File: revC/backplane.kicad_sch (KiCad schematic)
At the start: 40 parts, among them J101 BURN WIRES, J103 SEP1 & SEP2, J104 SEP3 & SEP4, J105 +X SOLAR PANEL, J106 -X SOLAR PANEL, J107 +Y SOLAR PANEL, J108 -Z SOLAR PANEL, J200_1 HSEC8-160-01-S-DV-A-K-TR, J200_2 HSEC8-160-01-S-DV-A-K-TR, J200_3 HSEC8-160-01-S-DV-A-K-TR, J200_4 HSEC8-160-01-S-DV-A-K-TR, J200_5 HSEC8-160-01-S-DV-A-K-TR, J200_6 HSEC8-160-01-S-DV-A-K-TR, J200_7 HSEC8-160-01-S-DV-A-K-TR, J200_8 HSEC8-160-01-S-DV-A-K-TR, J300 Breakout Connector, J301 Breakout Connector, SW100 RESET, SW101 RESET

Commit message: updated layout for fm.
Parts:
- removed J101: BURN WIRES, CubeSat_Backplane:SAMTEC_T1M-04-F-SV-L, symbol Connector_Generic:Conn_01x04
- added R604: 0R, Resistor_SMD:R_0402_1005Metric, symbol backplane-rescue:R_US-Device
- C100, C101, C102, C103, C104, C105: value 0.1uF -> 10nF; Manufacturer Part Number 1 GRM155R71C104KA88D -> CGA2B3X7S2A103K050BB
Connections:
- net H1-1 is gone; now on net SEP1_RET: J200_1.9 (Pin_9), J200_2.9 (Pin_9), J200_3.9 (Pin_9), J200_4.9 (Pin_9), J200_5.9 (Pin_9), J200_6.9 (Pin_9), J200_7.9 (Pin_9), J200_8.9 (Pin_9), J300.5 (Pin_5)
- net H1-16 is gone; now on net RBF_RET: J200_1.38 (Pin_38), J200_2.38 (Pin_38), J200_3.38 (Pin_38), J200_4.38 (Pin_38), J200_5.38 (Pin_38), J200_6.38 (Pin_38), J200_7.38 (Pin_38), J200_8.38 (Pin_38), J300.20 (Pin_20)
- net H1-2 is gone; now on net SEP2_RET: J200_1.10 (Pin_10), J200_2.10 (Pin_10), J200_3.10 (Pin_10), J200_4.10 (Pin_10), J200_5.10 (Pin_10), J200_6.10 (Pin_10), J200_7.10 (Pin_10), J200_8.10 (Pin_10), J300.6 (Pin_6)
- net H2-5 is gone; now on net GND: J200_1.19 (Pin_19), J200_2.19 (Pin_19), J200_3.19 (Pin_19), J200_4.19 (Pin_19), J200_5.19 (Pin_19), J200_6.19 (Pin_19), J200_7.19 (Pin_19), J200_8.19 (Pin_19), J301.9 (Pin_9)
- net H2-6 is gone; now on net GND: J200_1.20 (Pin_20), J200_2.20 (Pin_20), J200_3.20 (Pin_20), J200_4.20 (Pin_20), J200_5.20 (Pin_20), J200_6.20 (Pin_20), J200_7.20 (Pin_20), J200_8.20 (Pin_20), J301.10 (Pin_10)
- net DIN_LED_1: now also J200_1.14 (Pin_14), J301.8 (Pin_8); no longer J200_1.100 (Pin_100), J300.52 (Pin_52)
- net DIN_LED_2: now also J200_1.16 (Pin_16), J200_2.14 (Pin_14); no longer J200_1.102 (Pin_102), J200_2.100 (Pin_100)
- net DIN_LED_3: now also J200_2.16 (Pin_16), J200_3.14 (Pin_14); no longer J200_2.102 (Pin_102), J200_3.100 (Pin_100)
- net DIN_LED_4: now also J200_3.16 (Pin_16), J200_4.14 (Pin_14); no longer J200_3.102 (Pin_102), J200_4.100 (Pin_100)
- net DIN_LED_5: now also J200_4.16 (Pin_16), J200_5.14 (Pin_14); no longer J200_4.102 (Pin_102), J200_5.100 (Pin_100)
- net DIN_LED_6: now also J200_5.16 (Pin_16), J200_6.14 (Pin_14); no longer J200_5.102 (Pin_102), J200_6.100 (Pin_100)
- net DIN_LED_7: now also J200_6.16 (Pin_16), J200_7.14 (Pin_14); no longer J200_6.102 (Pin_102), J200_7.100 (Pin_100)
- net DIN_LED_8: now also J200_7.16 (Pin_16), J200_8.14 (Pin_14), R604.2; no longer J200_7.102 (Pin_102), J200_8.100 (Pin_100)
- net RBF_RET: no longer J200_1.107 (Pin_107), J200_2.107 (Pin_107), J200_3.107 (Pin_107), J200_4.107 (Pin_107), J200_5.107 (Pin_107), J200_6.107 (Pin_107), J200_7.107 (Pin_107), J200_8.107 (Pin_107), J301.53 (Pin_53)
- net SEP1_RET: no longer J200_1.109 (Pin_109), J200_2.109 (Pin_109), J200_3.109 (Pin_109), J200_4.109 (Pin_109), J200_5.109 (Pin_109), J200_6.109 (Pin_109), J200_7.109 (Pin_109), J200_8.109 (Pin_109), J300.55 (Pin_55)
- net SEP2_RET: no longer J200_1.110 (Pin_110), J200_2.110 (Pin_110), J200_3.110 (Pin_110), J200_4.110 (Pin_110), J200_5.110 (Pin_110), J200_6.110 (Pin_110), J200_7.110 (Pin_110), J200_8.110 (Pin_110), J300.56 (Pin_56)
- net BP_LED_PWR renamed H1-49
- net DIN_BO_LED renamed DIN_LED_BO
- net DIN_LED_BO: now also J300.8 (Pin_8); no longer J301.50 (Pin_50)
- net DIN_BP_LED renamed H1-48
- net H1-48: now also J200_1.102 (Pin_102), J200_2.102 (Pin_102), J200_3.102 (Pin_102), J200_4.102 (Pin_102), J200_5.102 (Pin_102), J200_6.102 (Pin_102), J200_7.102 (Pin_102), J300.52 (Pin_52)
- net H1-3 renamed ~{LED_EN}
- removed net H1-4: J200_1.14 (Pin_14), J200_2.14 (Pin_14), J200_3.14 (Pin_14), J200_4.14 (Pin_14), J200_5.14 (Pin_14), J200_6.14 (Pin_14), J200_7.14 (Pin_14), J200_8.14 (Pin_14), J300.8 (Pin_8)
- net H2-3 renamed LED_PWR
- removed net H2-4: J200_1.16 (Pin_16), J200_2.16 (Pin_16), J200_3.16 (Pin_16), J200_4.16 (Pin_16), J200_5.16 (Pin_16), J200_6.16 (Pin_16), J200_7.16 (Pin_16), J200_8.16 (Pin_16), J301.8 (Pin_8)
- net ~{BP_LED_EN} renamed H1-50
- new net DIN_LED_BP: J200_8.16 (Pin_16), R604.1
- new net H1-51: J200_1.109 (Pin_109), J200_2.109 (Pin_109), J200_3.109 (Pin_109), J200_4.109 (Pin_109), J200_5.109 (Pin_109), J200_6.109 (Pin_109), J200_7.109 (Pin_109), J200_8.109 (Pin_109), J300.55 (Pin_55)
- new net H1-52: J200_1.110 (Pin_110), J200_2.110 (Pin_110), J200_3.110 (Pin_110), J200_4.110 (Pin_110), J200_5.110 (Pin_110), J200_6.110 (Pin_110), J200_7.110 (Pin_110), J200_8.110 (Pin_110), J300.56 (Pin_56)
- new net H2-46: J200_1.100 (Pin_100), J200_2.100 (Pin_100), J200_3.100 (Pin_100), J200_4.100 (Pin_100), J200_5.100 (Pin_100), J200_6.100 (Pin_100), J200_7.100 (Pin_100), J200_8.100 (Pin_100), J301.50 (Pin_50)
- new net H2-49: J200_1.107 (Pin_107), J200_2.107 (Pin_107), J200_3.107 (Pin_107), J200_4.107 (Pin_107), J200_5.107 (Pin_107), J200_6.107 (Pin_107), J200_7.107 (Pin_107), J200_8.107 (Pin_107), J301.53 (Pin_53)
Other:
- note added: "Breakout Connectors"
- note added: "Breakout connectors are only used for ground testing. 2.1A per pin. trace width: 0.25mm Via: 0.2mm drill, 0.5mm dia."
- note added: "Bus Connectors"
- note added: "Configure pin on controller to have an internal pull up SELF_TEST input."
- note added: "DIN_LED-DOUT_LED jumpers install to bypass or stop data signal."
- note added: "LEDs"
- note added: "SK6812-EC3210 (NeoPixel) LEDs. Pull enable high at controller. LEDs are configured in a ring, with jumpers to bypass or terminate the data signal."
- note added: "Seperation Switch Connectors"
- note added: "Six #4 Mounting Holes for Sierra Lobo 1.5U cubesat structure."
- note added: "To connect breakout, connect male headers on rear of backplane then connect breakout harness (Samtec SFSD-30-28-G-15.74-D-NUS) Ensure harness is of "NUS" option for connecting to breakout."
- note removed: "BACKPLANE BREAKOUT CONNECTOR IS ONLY USED FOR GROUND TESTING CONTACT RATING 2.1A PER PIN TRACE WIDTH: 0.25mm VIA SIZE: 0.2mm DRILL, 0.5mm PAD"
- note removed: "Burn Wire Connector"
- note removed: "Configure pin on PPM/Motherboard/mainboard to have an internal pull up for H1-47 (USER0) for SELF_TEST input."
- note removed: "DIN_LED-DOUT_LED jumpers install when not used per backplane connector."
- note removed: "Default Bus Connectors"
- note removed: "End of CSK Bus"
- note removed: "First 104 pins follow pumpkin CSK bus (Rev E) pins Some user and IO pins have been assigned by SLI ( that are not used by any other peripherials )"
- note removed: "PCB BOTTOM"
- note removed: "PCB TOP"
- note removed: "Seperation Switch Connector"
- note removed: "breakout connectors are spaced such that the breakout BOARD thickness is 3.2mm!!"
- moved on the sheet: C100, C101, C102, C103, C104, C105, J103, J104, J105, J106, J107, J108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

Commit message: working post-review changes
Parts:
- added J1: SSM-102-L-SV-BE-TR, symbol Connector_Generic:Conn_01x02
- added J109: NTC1, SierraLobo:SAMTEC_T1M-02-F-SV-L-P, symbol Connector_Generic:Conn_01x02
- added J110: NTC2, SierraLobo:SAMTEC_T1M-02-F-SV-L-P, symbol Connector_Generic:Conn_01x02
- added J111: NTC3, SierraLobo:SAMTEC_T1M-02-F-SV-L-P, symbol Connector_Generic:Conn_01x02
- added J112: NTC4, SierraLobo:SAMTEC_T1M-02-F-SV-L-P, symbol Connector_Generic:Conn_01x02
- added J113: BURN1, SierraLobo:SAMTEC_T1M-04-F-SV-L, symbol Connector_Generic:Conn_01x04
- added J114: BURN2, SierraLobo:SAMTEC_T1M-04-F-SV-L, symbol Connector_Generic:Conn_01x04
- J103, J104: Manufacturer Part Number 1 (none) -> T1M-04-F-SV-L
- J105, J106, J107, J108: Manufacturer Part Number 1 (none) -> T1M-06-F-SV-L
- J200_1, J200_2, J200_3, J200_4, J200_5, J200_6, J200_7, J200_8: value HSEC8-160-01-S-DV-A-K-TR -> HTEC8-160-01-L-DV-A; Manufacturer Part Number 1 HSEC8-160-01-S-DV-A-K-TR -> HTEC8-160-01-L-DV-A
- MH100, MH101, MH102, MH103, MH104, MH105: Manufacturer Part Number 1 #4 Socket Head -> (none); now left out of the parts list
- R604: now not fitted
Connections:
- net H2-13 is gone; now on net GND: J200_1.35 (Pin_35), J200_2.35 (Pin_35), J200_3.35 (Pin_35), J200_4.35 (Pin_35), J200_5.35 (Pin_35), J200_6.35 (Pin_35), J200_7.35 (Pin_35), J200_8.35 (Pin_35), J301.17 (Pin_17)
- net H2-14 is gone; now on net GND: J200_1.36 (Pin_36), J200_2.36 (Pin_36), J200_3.36 (Pin_36), J200_4.36 (Pin_36), J200_5.36 (Pin_36), J200_6.36 (Pin_36), J200_7.36 (Pin_36), J200_8.36 (Pin_36), J301.18 (Pin_18)
- net H2-2 is gone; now on net SEP2_RET: J200_1.12 (Pin_12), J200_2.12 (Pin_12), J200_3.12 (Pin_12), J200_4.12 (Pin_12), J200_5.12 (Pin_12), J200_6.12 (Pin_12), J200_7.12 (Pin_12), J200_8.12 (Pin_12), J301.6 (Pin_6)
- net GND: now also J109.2 (Pin_2), J110.2 (Pin_2), J111.2 (Pin_2), J112.2 (Pin_2), J113.3 (Pin_3), J113.4 (Pin_4), J114.3 (Pin_3), J114.4 (Pin_4); no longer J200_1.19 (Pin_19), J200_1.20 (Pin_20), J200_2.19 (Pin_19), J200_2.20 (Pin_20), J200_3.19 (Pin_19), J200_3.20 (Pin_20), J200_4.19 (Pin_19), J200_4.20 (Pin_20), J200_5.19 (Pin_19), J200_5.20 (Pin_20), J200_6.19 (Pin_19), J200_6.20 (Pin_20), J200_7.19 (Pin_19), J200_7.20 (Pin_20), J200_8.19 (Pin_19), J200_8.20 (Pin_20), J301.10 (Pin_10), J301.9 (Pin_9)
- net RBF: now also J1.1 (Pin_1)
- net RBF_RET: now also J1.2 (Pin_2)
- net SEP1_RET: now also J200_1.13 (Pin_13), J200_2.13 (Pin_13), J200_3.13 (Pin_13), J200_4.13 (Pin_13), J200_5.13 (Pin_13), J200_6.13 (Pin_13), J200_7.13 (Pin_13), J200_8.13 (Pin_13), J300.7 (Pin_7); no longer J200_1.9 (Pin_9), J200_2.9 (Pin_9), J200_3.9 (Pin_9), J200_4.9 (Pin_9), J200_5.9 (Pin_9), J200_6.9 (Pin_9), J200_7.9 (Pin_9), J200_8.9 (Pin_9), J300.5 (Pin_5)
- net SEP2_RET: no longer J200_1.10 (Pin_10), J200_2.10 (Pin_10), J200_3.10 (Pin_10), J200_4.10 (Pin_10), J200_5.10 (Pin_10), J200_6.10 (Pin_10), J200_7.10 (Pin_10), J200_8.10 (Pin_10), J300.6 (Pin_6)
- net ~{LED_EN}: no longer J200_1.13 (Pin_13), J200_2.13 (Pin_13), J200_3.13 (Pin_13), J200_4.13 (Pin_13), J200_5.13 (Pin_13), J200_6.13 (Pin_13), J200_7.13 (Pin_13), J200_8.13 (Pin_13), J300.7 (Pin_7)
- net H2-7 renamed NTC3
- net NTC3: now also J111.1 (Pin_1)
- net H2-8 renamed NTC4
- net NTC4: now also J112.1 (Pin_1)
- new net NTC1: J109.1 (Pin_1), J200_1.19 (Pin_19), J200_2.19 (Pin_19), J200_3.19 (Pin_19), J200_4.19 (Pin_19), J200_5.19 (Pin_19), J200_6.19 (Pin_19), J200_7.19 (Pin_19), J200_8.19 (Pin_19), J301.9 (Pin_9)
- new net NTC2: J110.1 (Pin_1), J200_1.20 (Pin_20), J200_2.20 (Pin_20), J200_3.20 (Pin_20), J200_4.20 (Pin_20), J200_5.20 (Pin_20), J200_6.20 (Pin_20), J200_7.20 (Pin_20), J200_8.20 (Pin_20), J301.10 (Pin_10)
- new net VBURN1: J113.1 (Pin_1), J113.2 (Pin_2), J200_1.9 (Pin_9), J200_2.9 (Pin_9), J200_3.9 (Pin_9), J200_4.9 (Pin_9), J200_5.9 (Pin_9), J200_6.9 (Pin_9), J200_7.9 (Pin_9), J200_8.9 (Pin_9), J300.5 (Pin_5)
- new net VBURN2: J114.1 (Pin_1), J114.2 (Pin_2), J200_1.10 (Pin_10), J200_2.10 (Pin_10), J200_3.10 (Pin_10), J200_4.10 (Pin_10), J200_5.10 (Pin_10), J200_6.10 (Pin_10), J200_7.10 (Pin_10), J200_8.10 (Pin_10), J300.6 (Pin_6)
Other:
- note added: "Burn Wire Connectors"
- note added: "NTC Connectors"
- note added: "RBF Jumper"

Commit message: revC commit
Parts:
- removed J1: SSM-102-L-SV-BE-TR, symbol Connector_Generic:Conn_01x02
- added BOM1: RBF Jumper, symbol SierraLobo:BOMTIE
- added P100: RBF Terminal, SierraLobo:MilMax_0640-0, symbol Connector_Generic:Conn_01x01
- added P101: RBF_RET Terminal, SierraLobo:MilMax_0640-0, symbol Connector_Generic:Conn_01x01
- added R604 (x2): 0R, Resistor_SMD:R_0402_1005Metric, symbol backplane-rescue:R_US-Device
- J103, J104: footprint CubeSat_Backplane:SAMTEC_T1M-04-F-SV-L -> SierraLobo:SAMTEC_T1M-04-F-SV-L
- J105, J106, J107, J108: footprint CubeSat_Backplane:SAMTEC_T1M-06-F-SV-L -> SierraLobo:SAMTEC_T1M-06-F-SV-L
- J200_1, J200_2, J200_3, J200_4, J200_5, J200_6, J200_7, J200_8: footprint CubeSat_Backplane:HSEC8-160-01-S-DV-A-K-TR -> SierraLobo:HSEC8-160-01-S-DV-A-K-TR
- J300, J301: footprint CubeSat_Backplane:SAMTEC_CLP-130-02-X-D-BE-A-P-TR -> SierraLobo:SAMTEC_CLP-130-02-X-D-BE-A-P-TR
- MH100, MH101, MH102, MH103, MH104, MH105: footprint CubeSat_Backplane:#4_PTH -> SierraLobo:#4_PTH
- R100: value 0mR DNP -> 0R; footprint Resistor_SMD:R_0603_1608Metric -> Resistor_SMD:R_1206_3216Metric; Manufacturer Part Number 1 RC0603JR-070RL -> Keystone 5108
- R604: now fitted
- SW100, SW101: footprint CubeSat_Backplane:KMT031_NGJ_LHS -> SierraLobo:KMT031_NGJ_LHS
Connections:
- net BUS_RESET: now also R604.2; no longer SW100.2
- net RBF: now also P100.1 (Pin_1)
- net RBF_RET: now also P101.1 (Pin_1)
- net SELF_TEST: now also R604.2; no longer SW101.2
- new net: R604.1, SW100.2
- new net: R604.1, SW101.2
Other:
- moved on the sheet: SW100, SW101

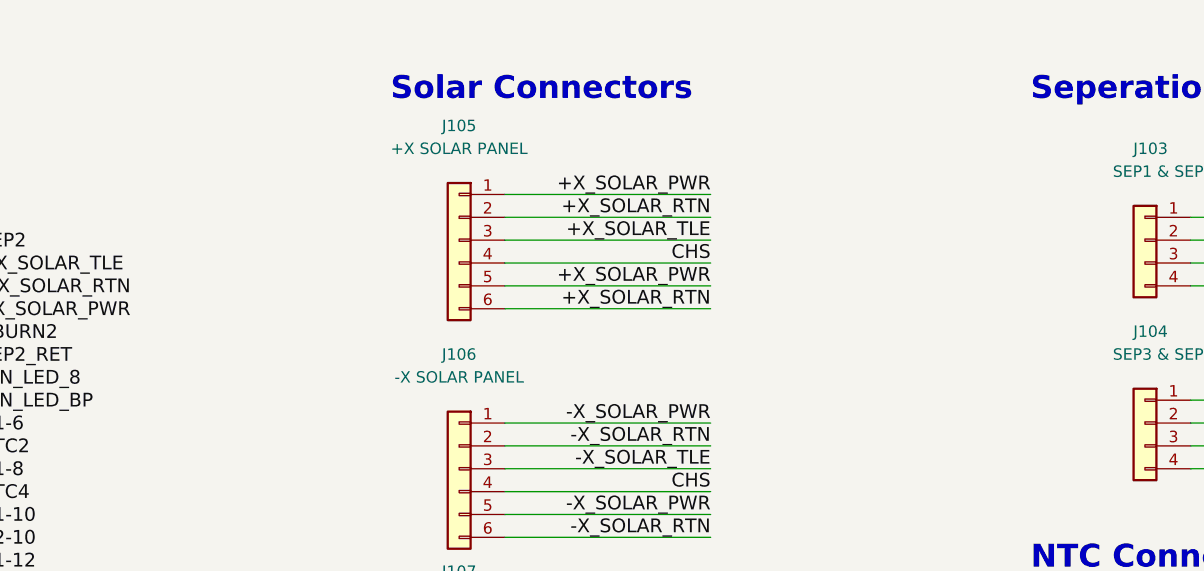
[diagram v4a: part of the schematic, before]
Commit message: added some datasheets
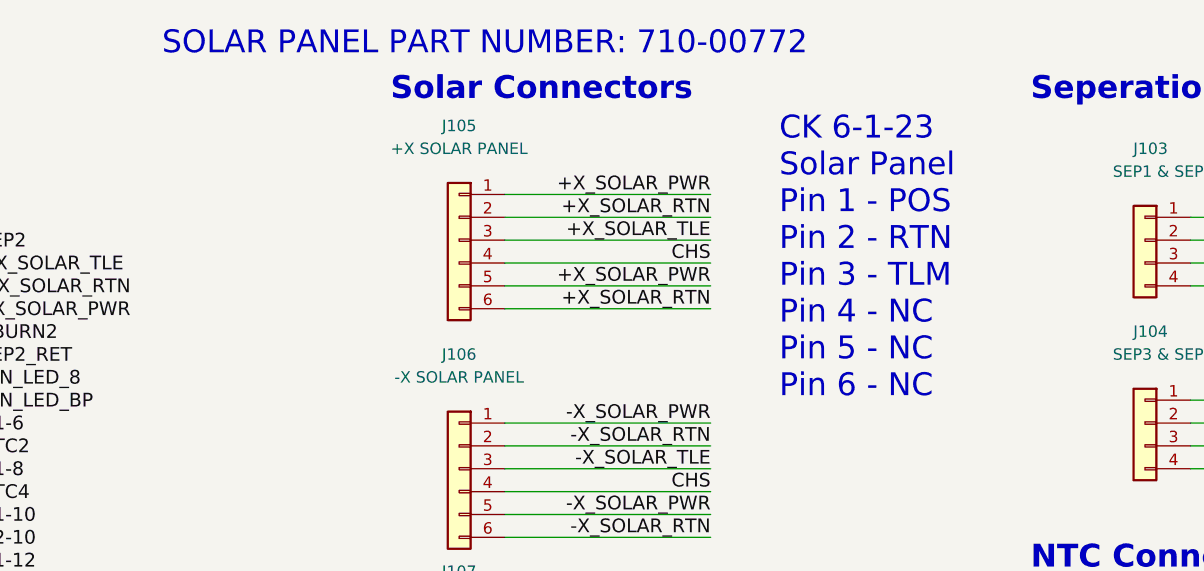
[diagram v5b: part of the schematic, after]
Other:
- note added: "CK 6-1-23 Solar Panel Pin 1 - POS Pin 2 - RTN Pin 3 - TLM Pin 4 - NC Pin 5 - NC Pin 6 - NC"
- note added: "SOLAR PANEL PART NUMBER: 710-00772"
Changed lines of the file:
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@@
     (effects (font (size 1.27 1.27)) (justify left bottom))
+  )
+  (text "SOLAR PANEL PART NUMBER: 710-00772" (at 266.7 17.78 0)
+    (effects (font (size 2.54 2.54)) (justify left bottom))
   )
   (text "Burn Wire Connectors" (at 454.66 22.86 0)
@@
     (effects (font (size 2.54 2.54)) (justify left bottom))
   )
+  (text "CK 6-1-23\nSolar Panel \nPin 1 - POS\nPin 2 - RTN\nPin 3 - TLM\nPin 4 - NC\nPin 5 - NC\nPin 6 - NC"
+    (at 335.28 55.88 0)
+    (effects (font (size 2.54 2.54)) (justify left bottom))
+  )

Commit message: retrieved original revC, latest is now C1
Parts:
- removed BOM1: RBF Jumper, symbol SierraLobo:BOMTIE
- removed J109: NTC1, SierraLobo:SAMTEC_T1M-02-F-SV-L-P, symbol Connector_Generic:Conn_01x02
- removed J110: NTC2, SierraLobo:SAMTEC_T1M-02-F-SV-L-P, symbol Connector_Generic:Conn_01x02
- removed J111: NTC3, SierraLobo:SAMTEC_T1M-02-F-SV-L-P, symbol Connector_Generic:Conn_01x02
- removed J112: NTC4, SierraLobo:SAMTEC_T1M-02-F-SV-L-P, symbol Connector_Generic:Conn_01x02
- removed J113: BURN1, SierraLobo:SAMTEC_T1M-04-F-SV-L, symbol Connector_Generic:Conn_01x04
- removed J114: BURN2, SierraLobo:SAMTEC_T1M-04-F-SV-L, symbol Connector_Generic:Conn_01x04
- removed P100: RBF Terminal, SierraLobo:MilMax_0640-0, symbol Connector_Generic:Conn_01x01
- removed P101: RBF_RET Terminal, SierraLobo:MilMax_0640-0, symbol Connector_Generic:Conn_01x01
- removed R604 (x11): 0R, Resistor_SMD:R_0402_1005Metric, symbol backplane-rescue:R_US-Device
- added J101: BURN WIRES, CubeSat_Backplane:SAMTEC_T1M-04-F-SV-L, symbol Connector_Generic:Conn_01x04
- C100, C101, C102, C103, C104, C105: value 10nF -> 0.1uF; Manufacturer Part Number 1 CGA2B3X7S2A103K050BB -> GRM155R71C104KA88D
- J103, J104: footprint SierraLobo:SAMTEC_T1M-04-F-SV-L -> CubeSat_Backplane:SAMTEC_T1M-04-F-SV-L; Manufacturer Part Number 1 T1M-04-F-SV-L -> (none)
- J105, J106, J107, J108: footprint SierraLobo:SAMTEC_T1M-06-F-SV-L -> CubeSat_Backplane:SAMTEC_T1M-06-F-SV-L; Manufacturer Part Number 1 T1M-06-F-SV-L -> (none)
- J200_1, J200_2, J200_3, J200_4, J200_5, J200_6, J200_7, J200_8: value HTEC8-160-01-L-DV-A -> HSEC8-160-01-S-DV-A-K-TR; footprint SierraLobo:HSEC8-160-01-S-DV-A-K-TR -> CubeSat_Backplane:HSEC8-160-01-S-DV-A-K-TR; Manufacturer Part Number 1 HTEC8-160-01-L-DV-A -> HSEC8-160-01-S-DV-A-K-TR
- J300, J301: footprint SierraLobo:SAMTEC_CLP-130-02-X-D-BE-A-P-TR -> CubeSat_Backplane:SAMTEC_CLP-130-02-X-D-BE-A-P-TR
- MH100, MH101, MH102, MH103, MH104, MH105: footprint SierraLobo:#4_PTH -> CubeSat_Backplane:#4_PTH; Manufacturer Part Number 1 (none) -> #4 Socket Head; now in the parts list
- R100: value 0R -> 0mR DNP; footprint Resistor_SMD:R_1206_3216Metric -> Resistor_SMD:R_0603_1608Metric; Manufacturer Part Number 1 Keystone 5108 -> RC0603JR-070RL
- SW100, SW101: footprint SierraLobo:KMT031_NGJ_LHS -> CubeSat_Backplane:KMT031_NGJ_LHS
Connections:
- net DIN_LED_BO is gone; now on net H1-4: J300.8 (Pin_8)
- net DIN_LED_BP is gone; now on net H2-4: J200_8.16 (Pin_16)
- net H1-51 is gone; now on net SEP1_RET: J200_1.109 (Pin_109), J200_2.109 (Pin_109), J200_3.109 (Pin_109), J200_4.109 (Pin_109), J200_5.109 (Pin_109), J200_6.109 (Pin_109), J200_7.109 (Pin_109), J200_8.109 (Pin_109), J300.55 (Pin_55)
- net H1-52 is gone; now on net SEP2_RET: J200_1.110 (Pin_110), J200_2.110 (Pin_110), J200_3.110 (Pin_110), J200_4.110 (Pin_110), J200_5.110 (Pin_110), J200_6.110 (Pin_110), J200_7.110 (Pin_110), J200_8.110 (Pin_110), J300.56 (Pin_56)
- net +X_SOLAR_PWR: now also J105.2 (Pin_2); no longer J105.1 (Pin_1), J105.5 (Pin_5)
- net +X_SOLAR_RTN: now also J105.1 (Pin_1); no longer J105.2 (Pin_2), J105.6 (Pin_6)
- net +Y_SOLAR_PWR: now also J107.2 (Pin_2); no longer J107.1 (Pin_1), J107.5 (Pin_5)
- net +Y_SOLAR_RTN: now also J107.1 (Pin_1); no longer J107.2 (Pin_2), J107.6 (Pin_6)
- net -X_SOLAR_PWR: now also J106.2 (Pin_2); no longer J106.1 (Pin_1), J106.5 (Pin_5)
- net -X_SOLAR_RTN: now also J106.1 (Pin_1); no longer J106.2 (Pin_2), J106.6 (Pin_6)
- net -Z_SOLAR_PWR: now also J108.2 (Pin_2); no longer J108.1 (Pin_1), J108.5 (Pin_5)
- net -Z_SOLAR_RTN: now also J108.1 (Pin_1); no longer J108.2 (Pin_2), J108.6 (Pin_6)
- net BUS_RESET: now also SW100.2
- net CHS: now also J105.6 (Pin_6), J106.6 (Pin_6), J107.6 (Pin_6), J108.6 (Pin_6); no longer J105.4 (Pin_4), J106.4 (Pin_4), J107.4 (Pin_4), J108.4 (Pin_4)
- net GND: now also J105.4 (Pin_4), J105.5 (Pin_5), J106.4 (Pin_4), J106.5 (Pin_5), J107.4 (Pin_4), J107.5 (Pin_5), J108.4 (Pin_4), J108.5 (Pin_5), J101.3 (Pin_3), J101.4 (Pin_4); no longer J200_1.35 (Pin_35), J200_1.36 (Pin_36), J200_2.35 (Pin_35), J200_2.36 (Pin_36), J200_3.35 (Pin_35), J200_3.36 (Pin_36), J200_4.35 (Pin_35), J200_4.36 (Pin_36), J200_5.35 (Pin_35), J200_5.36 (Pin_36), J200_6.35 (Pin_35), J200_6.36 (Pin_36), J200_7.35 (Pin_35), J200_7.36 (Pin_36), J200_8.35 (Pin_35), J200_8.36 (Pin_36), J301.17 (Pin_17), J301.18 (Pin_18)
- net SELF_TEST: now also SW101.2
- net SEP1_RET: no longer J200_1.13 (Pin_13), J200_2.13 (Pin_13), J200_3.13 (Pin_13), J200_4.13 (Pin_13), J200_5.13 (Pin_13), J200_6.13 (Pin_13), J200_7.13 (Pin_13), J200_8.13 (Pin_13), J300.7 (Pin_7)
- net SEP2_RET: no longer J200_1.12 (Pin_12), J200_2.12 (Pin_12), J200_3.12 (Pin_12), J200_4.12 (Pin_12), J200_5.12 (Pin_12), J200_6.12 (Pin_12), J200_7.12 (Pin_12), J200_8.12 (Pin_12), J301.6 (Pin_6)
- net DIN_LED_1 renamed H1-4
- net H1-4: now also J200_2.14 (Pin_14), J200_3.14 (Pin_14), J200_4.14 (Pin_14), J200_5.14 (Pin_14), J200_6.14 (Pin_14), J200_7.14 (Pin_14), J200_8.14 (Pin_14); no longer J301.8 (Pin_8)
- net DIN_LED_2 renamed H2-4
- net H2-4: now also J200_2.16 (Pin_16), J200_3.16 (Pin_16), J200_4.16 (Pin_16), J200_5.16 (Pin_16), J200_6.16 (Pin_16), J200_7.16 (Pin_16), J301.8 (Pin_8); no longer J200_2.14 (Pin_14)
- removed net DIN_LED_3: J200_2.16 (Pin_16), J200_3.14 (Pin_14)
- removed net DIN_LED_4: J200_3.16 (Pin_16), J200_4.14 (Pin_14)
- removed net DIN_LED_5: J200_4.16 (Pin_16), J200_5.14 (Pin_14)
- removed net DIN_LED_6: J200_5.16 (Pin_16), J200_6.14 (Pin_14)
- removed net DIN_LED_7: J200_6.16 (Pin_16), J200_7.14 (Pin_14)
- removed net DIN_LED_8: J200_7.16 (Pin_16), J200_8.14 (Pin_14)
- net H1-48 renamed USER_1
- net H1-49 renamed USER_2
- net H1-50 renamed USER_3
- net LED_PWR renamed H2-3
- net NTC1 renamed H2-5
- net NTC2 renamed H2-6
- net NTC3 renamed H2-7
- net NTC4 renamed H2-8
- net RBF_RET renamed H1-16
- net VBURN1 renamed H1-1
- net H1-1: now also J101.1 (Pin_1)
- net VBURN2 renamed H1-2
- net H1-2: now also J101.2 (Pin_2)
- new net H1-3: J200_1.13 (Pin_13), J200_2.13 (Pin_13), J200_3.13 (Pin_13), J200_4.13 (Pin_13), J200_5.13 (Pin_13), J200_6.13 (Pin_13), J200_7.13 (Pin_13), J200_8.13 (Pin_13), J300.7 (Pin_7)
- new net H2-13: J200_1.35 (Pin_35), J200_2.35 (Pin_35), J200_3.35 (Pin_35), J200_4.35 (Pin_35), J200_5.35 (Pin_35), J200_6.35 (Pin_35), J200_7.35 (Pin_35), J200_8.35 (Pin_35), J301.17 (Pin_17)
- new net H2-14: J200_1.36 (Pin_36), J200_2.36 (Pin_36), J200_3.36 (Pin_36), J200_4.36 (Pin_36), J200_5.36 (Pin_36), J200_6.36 (Pin_36), J200_7.36 (Pin_36), J200_8.36 (Pin_36), J301.18 (Pin_18)
- new net H2-2: J200_1.12 (Pin_12), J200_2.12 (Pin_12), J200_3.12 (Pin_12), J200_4.12 (Pin_12), J200_5.12 (Pin_12), J200_6.12 (Pin_12), J200_7.12 (Pin_12), J200_8.12 (Pin_12), J301.6 (Pin_6)
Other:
- sheet LED Driver ports: added 5V_USB; removed DOUT, GND, LED_PWR, ~{LED_EN}
- note added: "BACKPLANE BREAKOUT CONNECTOR IS ONLY USED FOR GROUND TESTING CONTACT RATING 2.1A PER PIN TRACE WIDTH: 0.25mm VIA SIZE: 0.2mm DRILL, 0.5mm PAD"
- note added: "Burn Wire Connector"
- note added: "Configure pin on PPM/Motherboard/mainboard to have an internal pull up for H1-47 (USER0) for SELF_TEST input."
- note added: "Default Bus Connectors"
- note added: "End of CSK Bus"
- note added: "First 104 pins follow pumpkin CSK bus (Rev E) pins Some user and IO pins have been assigned by SLI ( that are not used by any other peripherials )"
- note added: "LED Driver"
- note added: "PCB BOTTOM"
- note added: "PCB TOP"
- note added: "SIN and SCLK are connected to the SDO0 and SCK0 pins on the bus respectively USER_1 (active high) not only activates the latch on U600-601 but allows serial data to pass to them"
- note added: "Seperation Switch Connector"
- note added: "breakout connectors are spaced such that the breakout BOARD thickness is 3.2mm!!"
- note removed: "Breakout Connectors"
- note removed: "Breakout connectors are only used for ground testing. 2.1A per pin. trace width: 0.25mm Via: 0.2mm drill, 0.5mm dia."
- note removed: "Burn Wire Connectors"
- note removed: "Bus Connectors"
- note removed: "CK 6-1-23 Solar Panel Pin 1 - POS Pin 2 - RTN Pin 3 - TLM Pin 4 - NC Pin 5 - NC Pin 6 - NC"
- note removed: "Configure pin on controller to have an internal pull up SELF_TEST input."
- note removed: "DIN_LED-DOUT_LED jumpers install to bypass or stop data signal."
- note removed: "DNP"
- note removed: "LEDs"
- note removed: "NTC Connectors"
- note removed: "RBF Jumper"
- note removed: "SK6812-EC3210 (NeoPixel) LEDs. Pull enable high at controller. LEDs are configured in a ring, with jumpers to bypass or terminate the data signal."
- note removed: "SOLAR PANEL PART NUMBER: 710-00772"
- note removed: "Seperation Switch Connectors"
- note removed: "Six #4 Mounting Holes for Sierra Lobo 1.5U cubesat structure."
- note removed: "To connect breakout, connect male headers on rear of backplane then connect breakout harness (Samtec SFSD-30-28-G-15.74-D-NUS) Ensure harness is of "NUS" option for connecting to breakout."
- moved on the sheet: C100, C101, C102, C103, C104, C105, J103, J104, J105, J106, J107, J108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
